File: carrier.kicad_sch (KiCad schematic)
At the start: 29 parts, among them J1 Conn_02x06_Odd_Even, J2 Conn_01x26, J3 Conn_01x26, U1 CARAVEL, U2 W25Q128JVS, U3 LP5907MFX-3.3, U4 LP5907MFX-1.8, U5 LP5907MFX-1.8, U6 LP5907MFX-3.3, X1 SG-5032CAN

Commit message: Cleanup schematics by dividing it into relevant sections
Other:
- note added: "Clock"
- note added: "Debug Port"
- note added: "Flash"
- note added: "Headers"
- note added: "Microcontroller"
- note added: "Power Section"
- moved on the sheet: C1, C10, C11, C12, C13, C14, C15, C16, C2, C3, C4, C5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

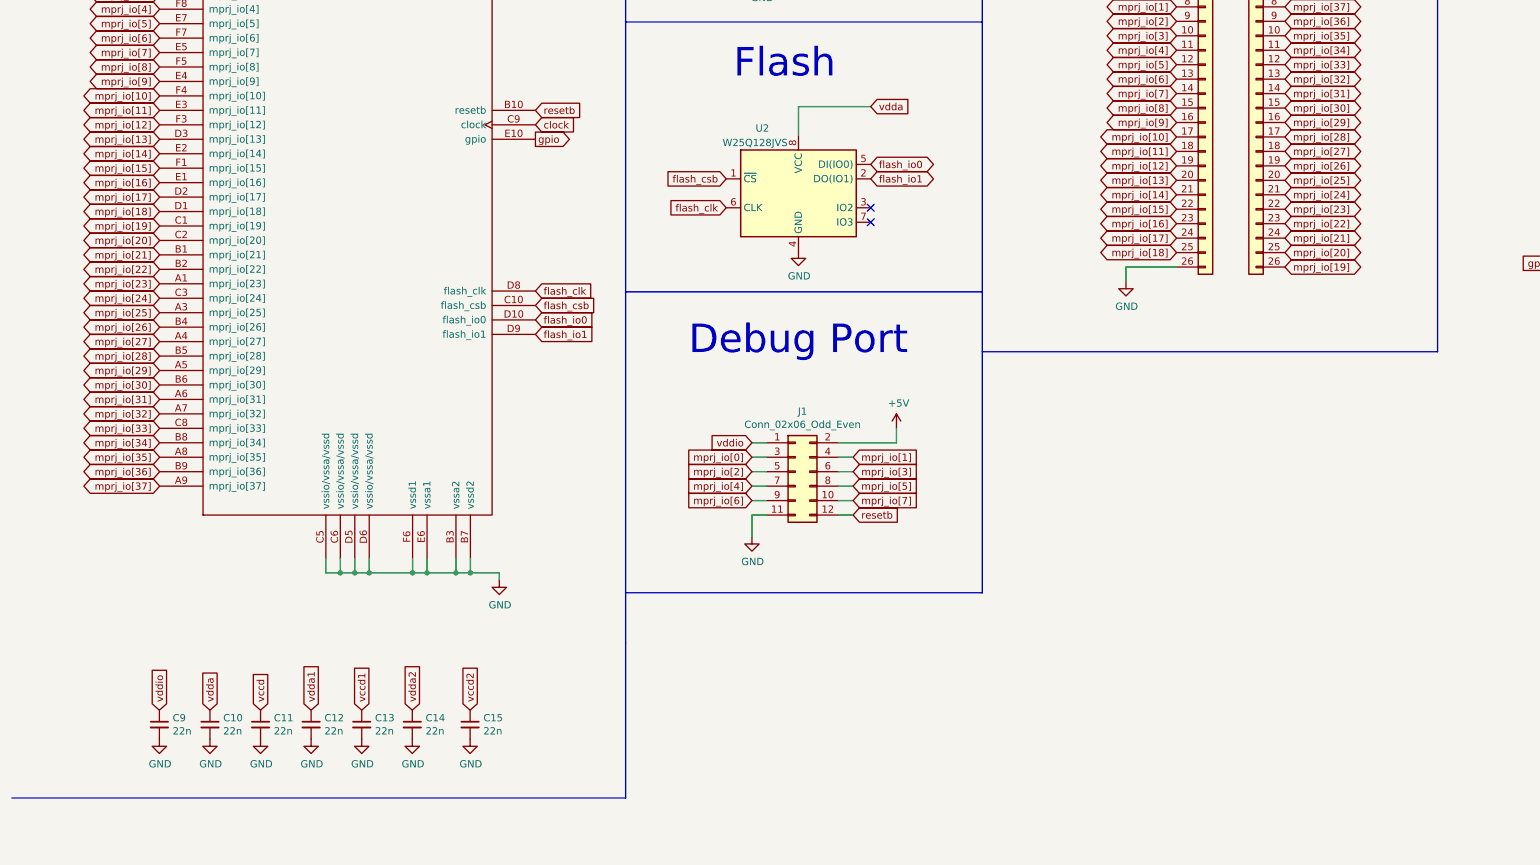
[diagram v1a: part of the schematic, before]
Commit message: Added schematics for USB Section
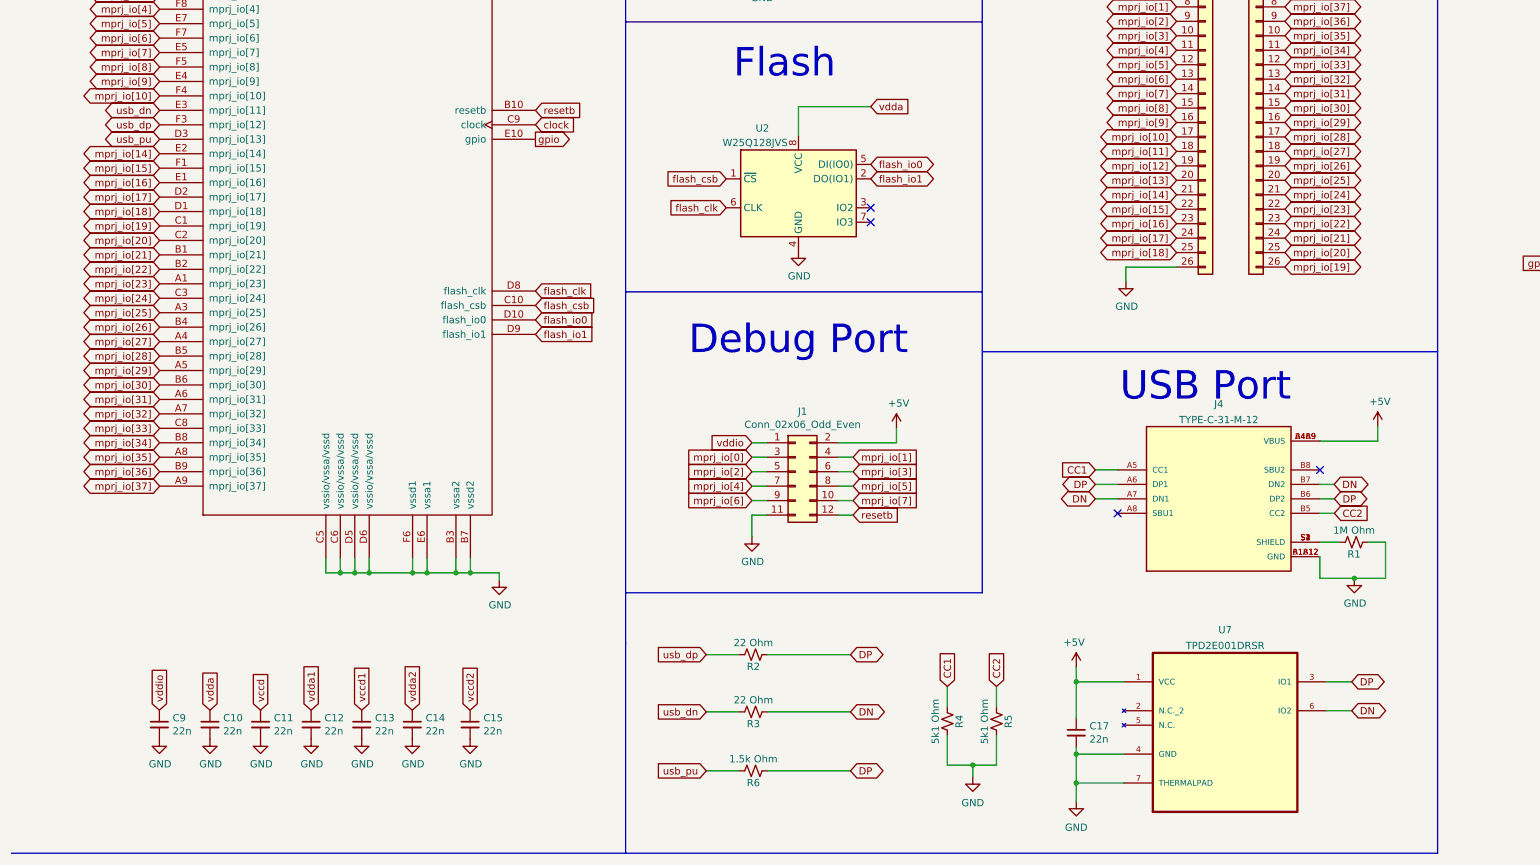
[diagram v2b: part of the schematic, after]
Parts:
- added C17: 22n, Capacitor_SMD:C_0402_1005Metric, symbol Device:C_Small
- added J4: TYPE-C-31-M-12, HRO_TYPE-C-31-M-12, symbol TYPE-C-31-M-12:TYPE-C-31-M-12
- added R1: 1M Ohm, symbol Device:R_Small_US
- added R2, R3: 22 Ohm, symbol Device:R_Small_US
- added R4, R5: 5k1 Ohm, symbol Device:R_Small_US
- added R6: 1.5k Ohm, symbol Device:R_Small_US
- added U7: TPD2E001DRSR, SON95P315X315X80-7N, symbol TPD2E001DRSR:TPD2E001DRSR
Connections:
- net +5V: now also C17.1, J4.A4B9 (VBUS), J4.B4A9 (VBUS), U7.1 (VCC)
- net GND: now also C17.2, J4.A1B12 (GND), J4.B1A12 (GND), R1.2, R4.1, R5.1, U7.4 (GND), U7.7 (THERMALPAD)
- net mprj_io[11]: no longer U1.E3 (mprj_io[11])
- net mprj_io[12]: no longer U1.F3 (mprj_io[12])
- net mprj_io[13]: no longer U1.D3 (mprj_io[13])
- new net: J4.S1 (SHIELD), J4.S2 (SHIELD), J4.S3 (SHIELD), J4.S4 (SHIELD), R1.1
- new net CC1: J4.A5 (CC1), R4.2
- new net CC2: J4.B5 (CC2), R5.2
- new net DN: J4.A7 (DN1), J4.B7 (DN2), R3.2, U7.6 (IO2)
- new net DP: J4.A6 (DP1), J4.B6 (DP2), R2.2, R6.2, U7.3 (IO1)
- new net usb_dn: R3.1, U1.E3 (mprj_io[11])
- new net usb_dp: R2.1, U1.F3 (mprj_io[12])
- new net usb_pu: R6.1, U1.D3 (mprj_io[13])
- no-connect marks 3 -> 5
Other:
- note added: "USB Port"

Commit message: Switch to 2.54mm header for programming
Also imports changes from schematic to PCB.
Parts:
- J1: footprint Connector_PinHeader_1.27mm:PinHeader_2x06_P1.27mm_Vertical_SMD -> Connector_PinHeader_2.54mm:PinHeader_2x06_P2.54mm_Vertical
- R1, R2, R3, R4, R5, R6: footprint (none) -> Resistor_SMD:R_0402_1005Metric
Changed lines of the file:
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@@
     (property "Reference" "R2" (id 0) (at 142.494 172.4872 90))
     (property "Value" "22 Ohm" (id 1) (at 142.494 168.3027 90))
-    (property "Footprint" "" (id 2) (at 142.494 170.3832 0)
+    (property "Footprint" "Resistor_SMD:R_0402_1005Metric" (id 2) (at 142.494 170.3832 0)
       (effects (font (size 1.27 1.27)) hide)
     )
@@
     (property "Reference" "R3" (id 0) (at 142.494 182.5456 90))
     (property "Value" "22 Ohm" (id 1) (at 142.494 178.3611 90))
-    (property "Footprint" "" (id 2) (at 142.494 180.4416 0)
+    (property "Footprint" "Resistor_SMD:R_0402_1005Metric" (id 2) (at 142.494 180.4416 0)
       (effects (font (size 1.27 1.27)) hide)
     )
@@
     (property "Reference" "R6" (id 0) (at 142.494 192.9088 90))
     (property "Value" "1.5k Ohm" (id 1) (at 142.494 188.7243 90))
-    (property "Footprint" "" (id 2) (at 142.494 190.8048 0)
+    (property "Footprint" "Resistor_SMD:R_0402_1005Metric" (id 2) (at 142.494 190.8048 0)
       (effects (font (size 1.27 1.27)) hide)
     )
@@
     (property "Reference" "R4" (id 0) (at 178.6848 182.118 90))
     (property "Value" "5k1 Ohm" (id 1) (at 174.5003 182.118 90))
-    (property "Footprint" "" (id 2) (at 176.5808 182.118 0)
+    (property "Footprint" "Resistor_SMD:R_0402_1005Metric" (id 2) (at 176.5808 182.118 0)
       (effects (font (size 1.27 1.27)) hide)
     )
@@
     (property "Reference" "R5" (id 0) (at 187.3208 182.118 90))
     (property "Value" "5k1 Ohm" (id 1) (at 183.1363 182.118 90))
-    (property "Footprint" "" (id 2) (at 185.2168 182.118 0)
+    (property "Footprint" "Resistor_SMD:R_0402_1005Metric" (id 2) (at 185.2168 182.118 0)
       (effects (font (size 1.27 1.27)) hide)
     )
@@
     (property "Reference" "R1" (id 0) (at 248.0564 152.726 90))
     (property "Value" "1M Ohm" (id 1) (at 248.0564 148.5415 90))
-    (property "Footprint" "" (id 2) (at 248.0564 150.622 0)
+    (property "Footprint" "Resistor_SMD:R_0402_1005Metric" (id 2) (at 248.0564 150.622 0)
       (effects (font (size 1.27 1.27)) hide)
     )
@@
     (property "Reference" "J1" (id 0) (at 151.13 127.635 0))
     (property "Value" "Conn_02x06_Odd_Even" (id 1) (at 151.13 129.9464 0))
-    (property "Footprint" "Connector_PinHeader_1.27mm:PinHeader_2x06_P1.27mm_Vertical_SMD" (id 2) (at 149.86 138.2268 0)
+    (property "Footprint" "Connector_PinHeader_2.54mm:PinHeader_2x06_P2.54mm_Vertical" (id 2) (at 149.86 138.2268 0)
       (effects (font (size 1.27 1.27)) hide)
     )
@@
     )
     (path "/00000000-0000-0000-0000-00005fcd8a9b"
-      (reference "J1") (unit 1) (value "Conn_02x06_Odd_Even") (footprint "Connector_PinHeader_1.27mm:PinHeader_2x06_P1.27mm_Vertical_SMD")
+      (reference "J1") (unit 1) (value "Conn_02x06_Odd_Even") (footprint "Connector_PinHeader_2.54mm:PinHeader_2x06_P2.54mm_Vertical")
     )
     (path "/00000000-0000-0000-0000-00006003592e"
@@
     )
     (path "/d0b1a3a0-c53c-4f1f-bdfe-ed90ed8ca681"
-      (reference "R1") (unit 1) (value "1M Ohm") (footprint "")
+      (reference "R1") (unit 1) (value "1M Ohm") (footprint "Resistor_SMD:R_0402_1005Metric")
     )
     (path "/8ba0322a-c81d-4761-9993-3ef319eafd05"
-      (reference "R2") (unit 1) (value "22 Ohm") (footprint "")
+      (reference "R2") (unit 1) (value "22 Ohm") (footprint "Resistor_SMD:R_0402_1005Metric")
     )
     (path "/a2a028e4-3f91-4395-91c3-c9fb688adc0b"
-      (reference "R3") (unit 1) (value "22 Ohm") (footprint "")
+      (reference "R3") (unit 1) (value "22 Ohm") (footprint "Resistor_SMD:R_0402_1005Metric")
     )
     (path "/532fe851-fb00-4481-930a-b215ac1eda24"
-      (reference "R4") (unit 1) (value "5k1 Ohm") (footprint "")
+      (reference "R4") (unit 1) (value "5k1 Ohm") (footprint "Resistor_SMD:R_0402_1005Metric")
     )
     (path "/442f0d99-f00a-449d-b7d6-96302f112bf2"
-      (reference "R5") (unit 1) (value "5k1 Ohm") (footprint "")
+      (reference "R5") (unit 1) (value "5k1 Ohm") (footprint "Resistor_SMD:R_0402_1005Metric")
     )
     (path "/5033680f-4820-4395-aa03-a14458340da1"
-      (reference "R6") (unit 1) (value "1.5k Ohm") (footprint "")
+      (reference "R6") (unit 1) (value "1.5k Ohm") (footprint "Resistor_SMD:R_0402_1005Metric")
     )
     (path "/00000000-0000-0000-0000-00005fb81f59"

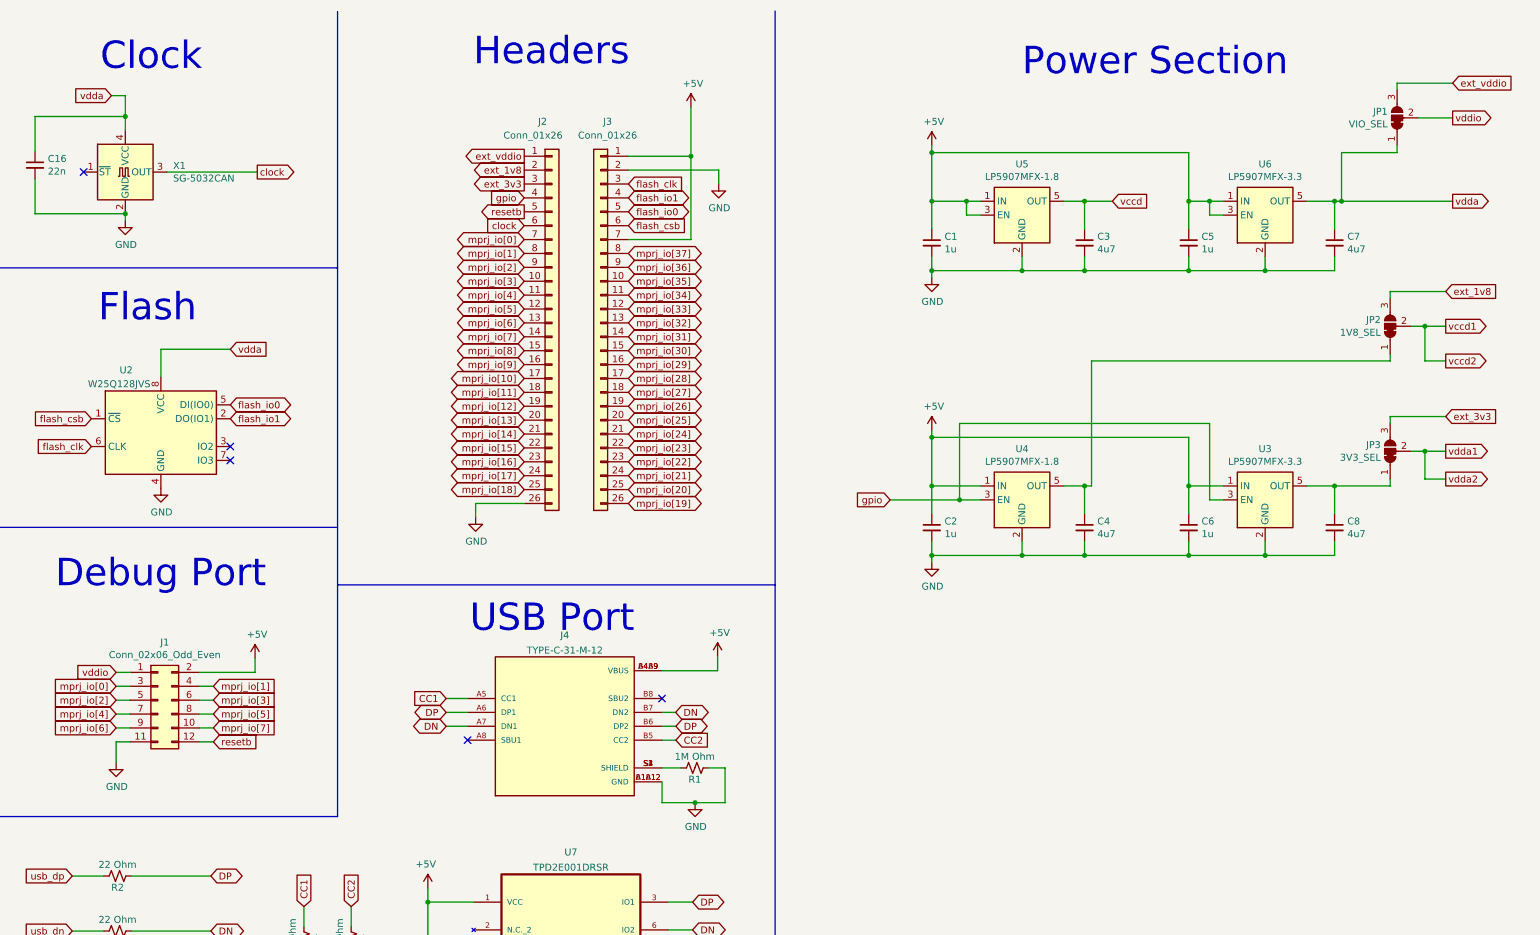
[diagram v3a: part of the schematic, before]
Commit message: Add current measurement jumpers
Removes solder bridges and adds jumpers for each power rail to measure current.
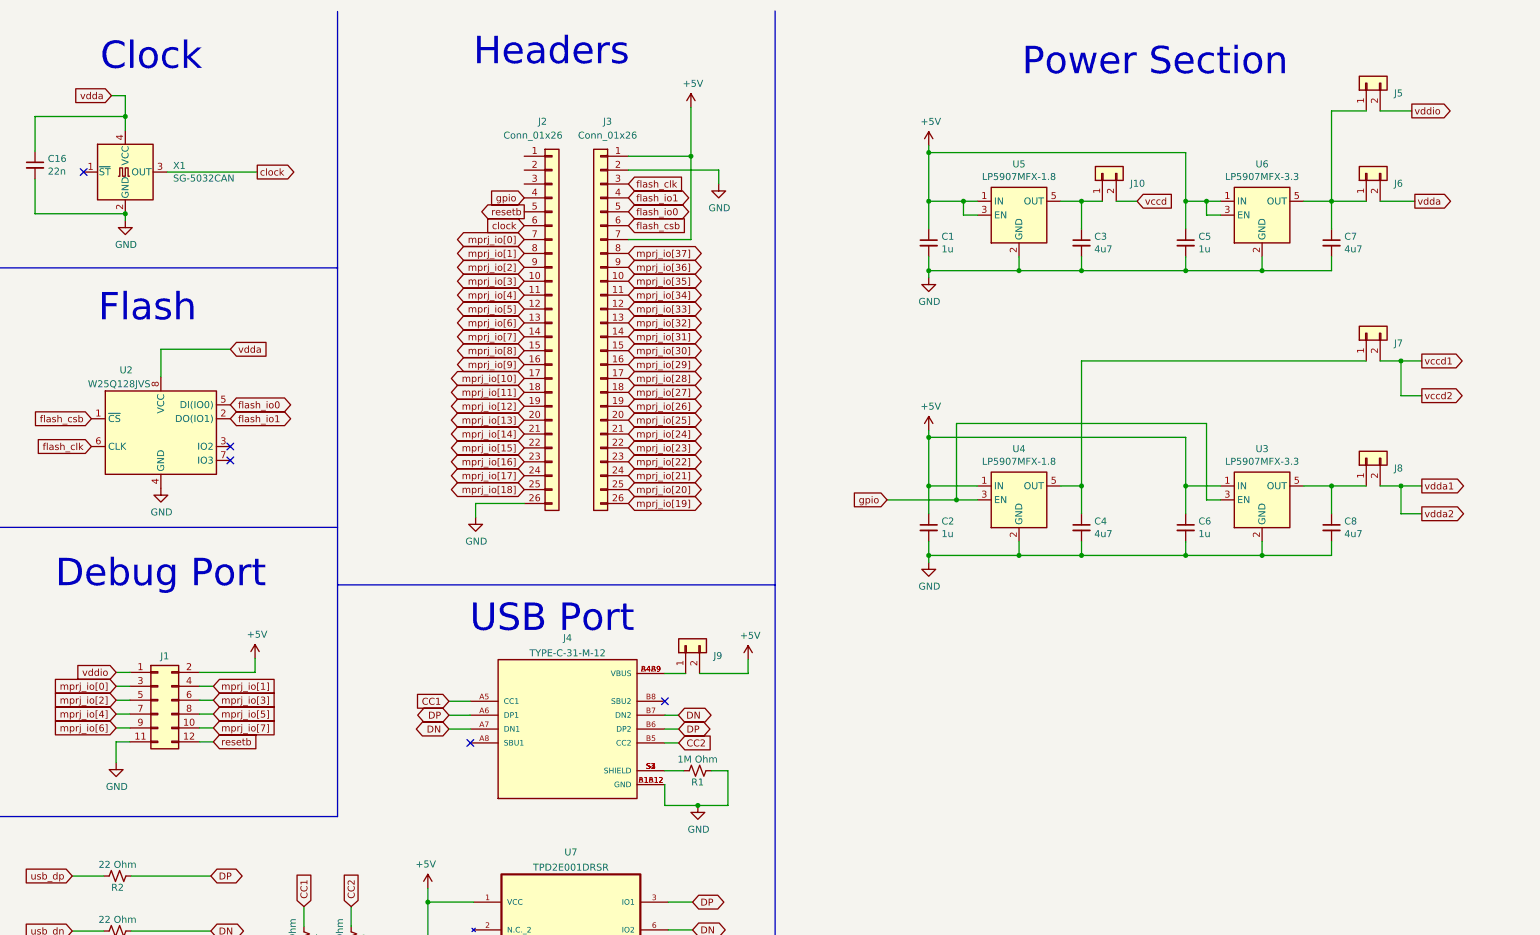
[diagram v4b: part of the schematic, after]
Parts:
- removed JP1: VIO_SEL, Jumper:SolderJumper-3_P1.3mm_Bridged12_Pad1.0x1.5mm, symbol Jumper:SolderJumper_3_Bridged12
- removed JP2: 1V8_SEL, Jumper:SolderJumper-3_P1.3mm_Bridged12_Pad1.0x1.5mm, symbol Jumper:SolderJumper_3_Bridged12
- removed JP3: 3V3_SEL, Jumper:SolderJumper-3_P1.3mm_Bridged12_Pad1.0x1.5mm, symbol Jumper:SolderJumper_3_Bridged12
- added J10, J5, J6, J7, J8, J9: Conn_01x02, Connector_PinHeader_2.54mm:PinHeader_1x02_P2.54mm_Vertical, symbol Connector_Generic:Conn_01x02
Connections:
- net +5V: now also J9.2 (Pin_2); no longer J4.A4B9 (VBUS), J4.B4A9 (VBUS)
- net vccd: now also J10.2 (Pin_2); no longer C3.1, U5.5 (OUT)
- net vccd1: now also J7.2 (Pin_2)
- net vdda: now also J6.2 (Pin_2); no longer C7.1, U6.5 (OUT)
- net vdda1: now also J8.2 (Pin_2)
- net vddio: now also J5.2 (Pin_2)
- net at C8.1, U3.5 (OUT): now also J8.1 (Pin_1)
- net at C4.1, U4.5 (OUT): now also J7.1 (Pin_1)
- net ext_1v8: no longer names the net of J2.2 (Pin_2)
- net ext_3v3: no longer names the net of J2.3 (Pin_3)
- net ext_vddio: no longer names the net of J2.1 (Pin_1)
- new net: C7.1, J5.1 (Pin_1), J6.1 (Pin_1), U6.5 (OUT)
- new net: C3.1, J10.1 (Pin_1), U5.5 (OUT)
- new net: J4.A4B9 (VBUS), J4.B4A9 (VBUS), J9.1 (Pin_1)
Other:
- moved on the sheet: C1, C2, C3, C4, C5, C6, C7, C8, J4, R1, U3, U4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
